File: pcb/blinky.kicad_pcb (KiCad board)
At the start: 2 copper layers, 80 x 30 mm, 13 parts, among them U1 ATtiny13A-SS

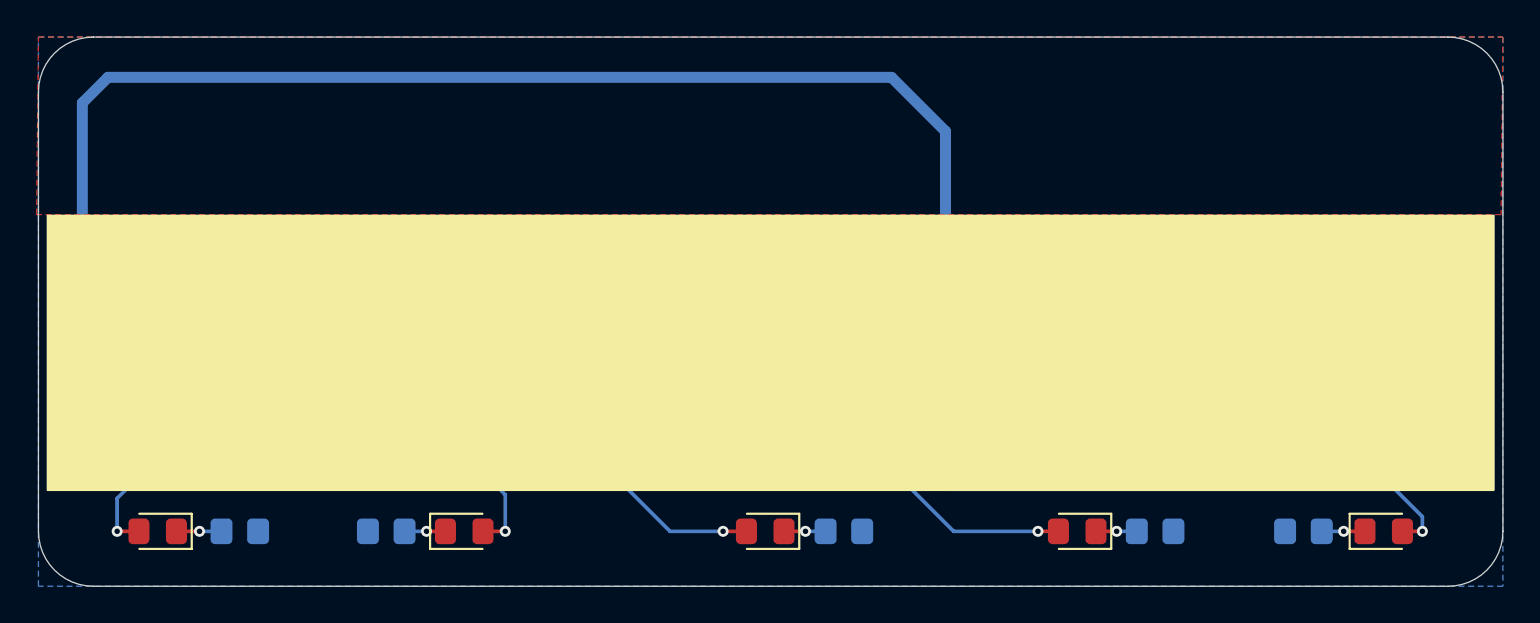
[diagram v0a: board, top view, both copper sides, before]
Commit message: Add website link to PCB
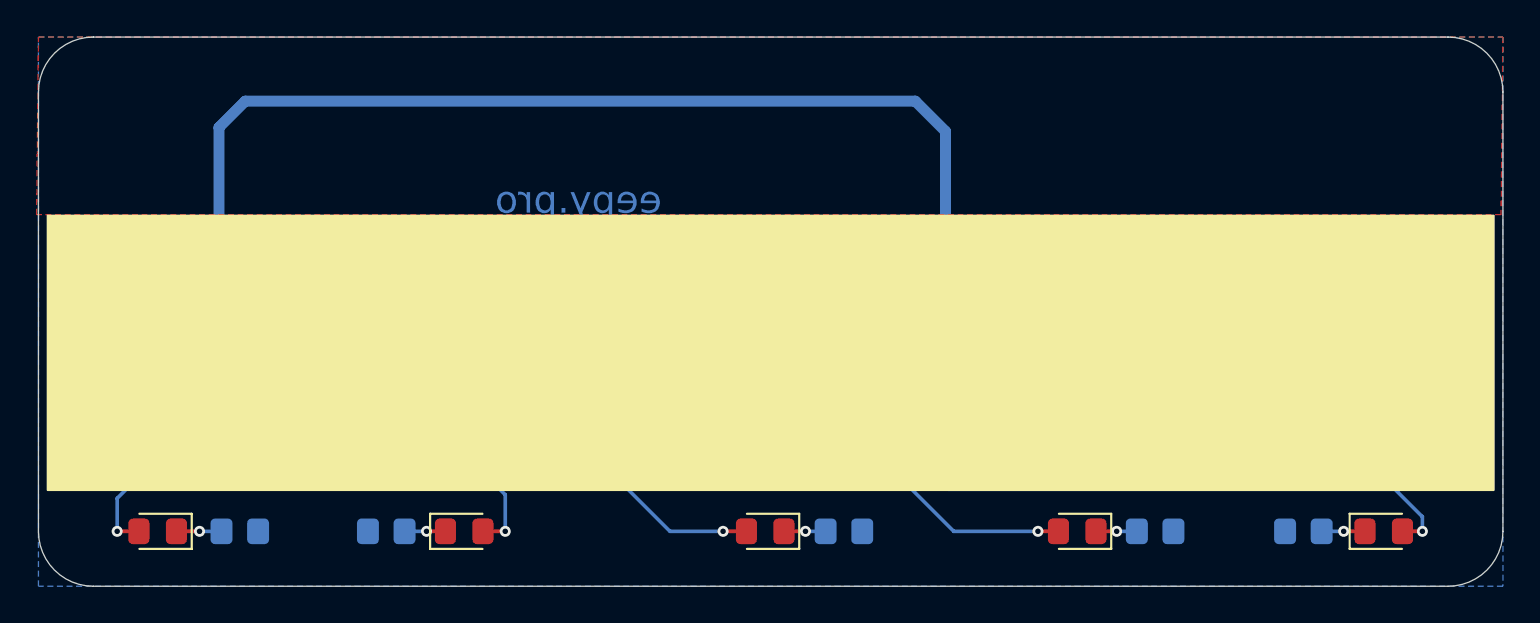
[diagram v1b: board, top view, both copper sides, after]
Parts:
- moved C1 0.14 mm to (75.0, 69.6)
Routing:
- net +BATT: track 76.4 -> 59.7 mm
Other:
- board text added: "eepy.pro"
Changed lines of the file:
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@@
 	(footprint "Capacitor_SMD:C_0805_2012Metric_Pad1.18x1.45mm_HandSolder"
 		(layer "B.Cu")
-		(at 74.9 69.5)
+		(at 75 69.6)
 		(descr "Capacitor SMD 0805 (2012 Metric), square (rectangular) end terminal, IPC_7351 nominal with elongated pad for handsoldering. (Body size source: IPC-SM-782 page 76, https://www.pcb-3d.com/wordpress/wp-content/uploads/ipc-sm-782a_amendment_1_and_2.pdf, https://docs.google.com/spreadsheets/d/1BsfQQcO9C6DZCsRaXUlFlo91Tg2WpOkGARC1WS5S8t0/edit?usp=sharing), generated with kicad-footprint-generator")
 		(tags "capacitor handsolder")
@@
 		)
 		(layer "Edge.Cuts")
+	)
+	(gr_text "eepy.pro"
+		(at 93.5 67.4 0)
+		(layer "B.Cu" knockout)
+		(effects
+			(font
+				(size 1.5 1.5)
+				(thickness 0.1875)
+			)
+			(justify mirror)
+		)
 	)
 	(gr_text "Hewwo~ my name is:"
@@
 	)
 	(segment
-		(start 66.4 62.1)
-		(end 66.4 70.5)
-		(width 0.6)
-		(layer "B.Cu")
-		(net 1)
-	)
-	(segment
-		(start 66.4 70.5)
-		(end 67.495 71.595)
+		(start 73.8625 63.4375)
+		(end 73.8625 69.5)
 		(width 0.6)
 		(layer "B.Cu")
@@
 	)
 	(segment
-		(start 72.525 69.75)
-		(end 72.775 69.5)
-		(width 0.5)
-		(layer "B.Cu")
-		(net 1)
-	)
-	(segment
 		(start 113.55 73)
 		(end 113.55 63.65)
@@
 	)
 	(segment
+		(start 72.675 69.6)
+		(end 73.9625 69.6)
+		(width 0.5)
+		(layer "B.Cu")
+		(net 1)
+	)
+	(segment
+		(start 111.9 62)
+		(end 75.3 62)
+		(width 0.6)
+		(layer "B.Cu")
+		(net 1)
+	)
+	(segment
+		(start 72.525 69.75)
+		(end 72.675 69.6)
+		(width 0.5)
+		(layer "B.Cu")
+		(net 1)
+	)
+	(segment
+		(start 75.3 62)
+		(end 73.8625 63.4375)
+		(width 0.6)
+		(layer "B.Cu")
+		(net 1)
+	)
+	(segment
 		(start 113.55 63.65)
-		(end 110.6 60.7)
-		(width 0.6)
-		(layer "B.Cu")
-		(net 1)
-	)
-	(segment
-		(start 72.775 69.5)
-		(end 73.7125 69.5)
-		(width 0.5)
-		(layer "B.Cu")
-		(net 1)
-	)
-	(segment
-		(start 67.495 71.595)
-		(end 72.525 71.595)
-		(width 0.6)
-		(layer "B.Cu")
-		(net 1)
-	)
-	(segment
-		(start 67.8 60.7)
-		(end 66.4 62.1)
-		(width 0.6)
-		(layer "B.Cu")
-		(net 1)
-	)
-	(segment
-		(start 110.6 60.7)
-		(end 67.8 60.7)
+		(end 111.9 62)
 		(width 0.6)
 		(layer "B.Cu")
@@
 	)
 	(segment
+		(start 74.7 79.7)
+		(end 74.7 75.2)
+		(width 0.2)
+		(layer "B.Cu")
+		(net 5)
+	)
+	(segment
+		(start 74.7 75.2)
+		(end 73.635 74.135)
+		(width 0.2)
+		(layer "B.Cu")
+		(net 5)
+	)
+	(segment
 		(start 89.5 85.5)
 		(end 89.5 83.5)
@@
 	)
 	(segment
-		(start 73.835 74.135)
-		(end 72.525 74.135)
+		(start 77 82)
+		(end 74.7 79.7)
 		(width 0.2)
 		(layer "B.Cu")
@@
 	)
 	(segment
-		(start 77 82)
-		(end 74.7 79.7)
-		(width 0.2)
-		(layer "B.Cu")
-		(net 5)
-	)
-	(segment
-		(start 74.7 79.7)
-		(end 74.7 75)
-		(width 0.2)
-		(layer "B.Cu")
-		(net 5)
-	)
-	(segment
-		(start 74.7 75)
-		(end 73.835 74.135)
+		(start 73.635 74.135)
+		(end 72.525 74.135)
 		(width 0.2)
 		(layer "B.Cu")
@@
 	)
 	(segment
+		(start 98.5 85.5)
+		(end 93.9 80.9)
+		(width 0.2)
+		(layer "B.Cu")
+		(net 7)
+	)
+	(segment
 		(start 101.4 85.5)
 		(end 98.5 85.5)
@@
 	)
 	(segment
+		(start 75.8 74.8)
+		(end 73.865 72.865)
+		(width 0.2)
+		(layer "B.Cu")
+		(net 7)
+	)
+	(segment
+		(start 93.9 80.9)
+		(end 77.6 80.9)
+		(width 0.2)
+		(layer "B.Cu")
+		(net 7)
+	)
+	(segment
+		(start 77.6 80.9)
+		(end 75.8 79.1)
+		(width 0.2)
+		(layer "B.Cu")
+		(net 7)
+	)
+	(segment
+		(start 73.865 72.865)
+		(end 72.525 72.865)
+		(width 0.2)
+		(layer "B.Cu")
+		(net 7)
+	)
+	(segment
 		(start 75.8 79.1)
 		(end 75.8 74.8)
 		(width 0.2)
 		(layer "B.Cu")
-		(net 7)
-	)
-	(segment
-		(start 73.865 72.865)
-		(end 72.525 72.865)
-		(width 0.2)
-		(layer "B.Cu")
-		(net 7)
-	)
-	(segment
-		(start 75.8 74.8)
-		(end 73.865 72.865)
-		(width 0.2)
-		(layer "B.Cu")
-		(net 7)
-	)
-	(segment
-		(start 77.6 80.9)
-		(end 75.8 79.1)
-		(width 0.2)
-		(layer "B.Cu")
-		(net 7)
-	)
-	(segment
-		(start 93.9 80.9)
-		(end 77.6 80.9)
-		(width 0.2)
-		(layer "B.Cu")
-		(net 7)
-	)
-	(segment
-		(start 98.5 85.5)
-		(end 93.9 80.9)
-		(width 0.2)
-		(layer "B.Cu")

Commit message: Add ISP header and LCSC part no.
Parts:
- added J1: ISP, JTAG:06x1_1.27mm, B.Cu at (67.1, 76.7)
- BT1: value Battery_Cell -> CR2032
- D1, D2, D3, D4, D5: value LED -> RED_LED
- R1, R2, R3, R4, R5: value R -> 220R
- U1: value ATtiny13A-SS -> ATtiny13A
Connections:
- net Net-(D1-A) renamed /MOSI
- net Net-(D2-A) renamed /MISO
- net Net-(D3-A) renamed /SCK
- U1 pad 1: Net-(U1-~{RESET}/PB5) -> /RST
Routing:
- net /RST: track 0.00 -> 11.8 mm, vias 0 -> 2
- net +BATT: track 59.7 -> 64.8 mm
- net /MOSI: track 13.0 -> 17.9 mm
- net /SCK: track 37.9 -> 42.7 mm
- net /MISO: track 26.7 -> 31.5 mm
- net GND: vias 0 -> 2
- added copper zone on F.Cu, net GND
- removed copper zone on F.Cu, net (none)

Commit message: Change font on PCB and remove dead site link
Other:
- board text added: "Hello, my name is:"
- board text removed: "Hewwo~ my name is:"
- board text removed: "eepy.pro"

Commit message: Clean up
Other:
- board text added: "Hewwo~ my name is:"
- board text removed: "Hello, my name is:"
